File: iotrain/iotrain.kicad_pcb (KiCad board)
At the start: 2 copper layers, 24 x 14 mm, 64 parts, among them J1 12V, J10 X2, J11 SCL, J12 SDA, J13 GND, J14 3V3, J15 GND, J2 PROG ESP, J3 AC1, J4 AC1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

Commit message: ESP32-C6
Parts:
- removed U1: ESP32-C3, Package_DFN_QFN:QFN-32-1EP_5x5mm_P0.5mm_EP3.7x3.7mm
- added C20: 10u/20V, Capacitor_SMD:C_0402_1005Metric, F.Cu at (139.9, 57.5)
- added C22: 10u/20V, Capacitor_SMD:C_0402_1005Metric, F.Cu at (139.0, 57.5)
- added J16: USB_B_Micro, Connector_USB:USB_Micro-B_Amphenol_10104110_Horizontal, B.Cu at (137.3, 63.6)
- added R10: 10k, Resistor_SMD:R_0201_0603Metric, F.Cu at (128.2, 65.5)
- added U4: ESP32-C6FH4, Package_DFN_QFN:QFN-32-1EP_5x5mm_P0.5mm_EP3.6x3.6mm, F.Cu at (130.9, 61.5)
- C11, C13: value 1u -> 10u/20V; footprint Capacitor_SMD:C_0201_0603Metric -> Capacitor_SMD:C_0402_1005Metric
- J2: moved to B.Cu
- L2: value L -> 2n
- moved C11 14.7 mm to (140.9, 57.5), turned to -90 degrees
- moved C13 7.12 mm to (138.1, 57.5), turned to -90 degrees
- moved R8 5.88 mm to (141.0, 61.1)
- moved R7 5.88 mm to (140.3, 61.1)
- moved SW2 5.84 mm to (136.4, 64.2), turned to 90 degrees
- moved U6 5.70 mm to (137.6, 56.8)
- moved C25 4.66 mm to (127.2, 62.4)
- moved C21 3.84 mm to (139.6, 61.1), turned to 90 degrees
- moved C14 3.61 mm to (135.4, 61.0)
- moved R1 3.54 mm to (134.3, 60.5), turned to 90 degrees
- moved C10 2.72 mm to (126.8, 61.4), turned to 90 degrees
- moved C12 2.23 mm to (125.8, 61.6), turned to 180 degrees
- moved SW1 2.09 mm to (139.7, 64.2), turned to 90 degrees
- moved C17 1.42 mm to (137.9, 53.6), turned to -90 degrees
- moved C15 1.30 mm to (137.9, 55.5), turned to -90 degrees
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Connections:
- net Net-(U1-LNA_IN) renamed ANT
- net PROG_IO0 renamed PROG_IO9
- C11 pad 1: +3V3 -> +12V
- C13 pad 1: +3V3 -> +12V
- J2 pad 1: PROG_EN -> CHIP_EN
- R1 pad 1: PROG_TX -> Net-(U4-U0TXD/GPIO16/FSPICS0)
- R1 pad 2: Net-(U1-U0TXD) -> PROG_TX
- R5 pad 1: GND -> unconnected-(R5-Pad1)
- R6 pad 2: Net-(U1-GPIO2) -> INFO_LED
- U6 pad 1: LCD_D -> unconnected-(U6-SDA-Pad1)
- U6 pad 10: GND -> unconnected-(U6-GND-Pad10)
- U6 pad 2: LCD_C -> unconnected-(U6-SCL-Pad2)
- U6 pad 3: LCD_RS -> unconnected-(U6-RS-Pad3)
- U6 pad 4: LCD_RES -> unconnected-(U6-RES-Pad4)
- U6 pad 5: LCD_CS -> unconnected-(U6-CS-Pad5)
- U6 pad 6: GND -> unconnected-(U6-GND-Pad6)
- U6 pad 7: +3V3 -> unconnected-(U6-VCC-Pad7)
- U6 pad 8: +3V3 -> unconnected-(U6-LEDA-Pad8)
- U6 pad 9: LCD_BL -> unconnected-(U6-LEDK-Pad9)
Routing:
- net MOT_IPROPRI: track 0.00 -> 15.0 mm, vias 0 -> 2
- net Net-(J16-D-): track 0.00 -> 6.36 mm, vias 0 -> 1
- net PROG_TX: track 2.47 -> 8.17 mm, vias 0 -> 1
- net PROG_IO9: track 0.00 -> 5.50 mm
- net INFO_LED: track 0.00 -> 4.96 mm, vias 0 -> 2
- net Net-(J16-D+): track 0.00 -> 4.91 mm, vias 0 -> 1
- net CHIP_EN: track 0.00 -> 4.25 mm, vias 0 -> 1
- net PROG_RX: track 5.88 -> 9.73 mm, vias 0 -> 1
- net +3V3: track 8.27 -> 11.9 mm, vias 0 -> 2
- net Net-(U1-U0TXD): track 3.09 -> 0.00 mm
- net Net-(U1-GPIO2): track 2.26 -> 0.00 mm, vias 2 -> 0
- net Net-(C9-Pad1): track 2.23 -> 0.00 mm
- net GND: track 4.00 -> 2.15 mm, vias 1 -> 0
- net PROG_EN: track 0.00 -> 1.66 mm
- net MOT_EN: track 10.5 -> 8.89 mm
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
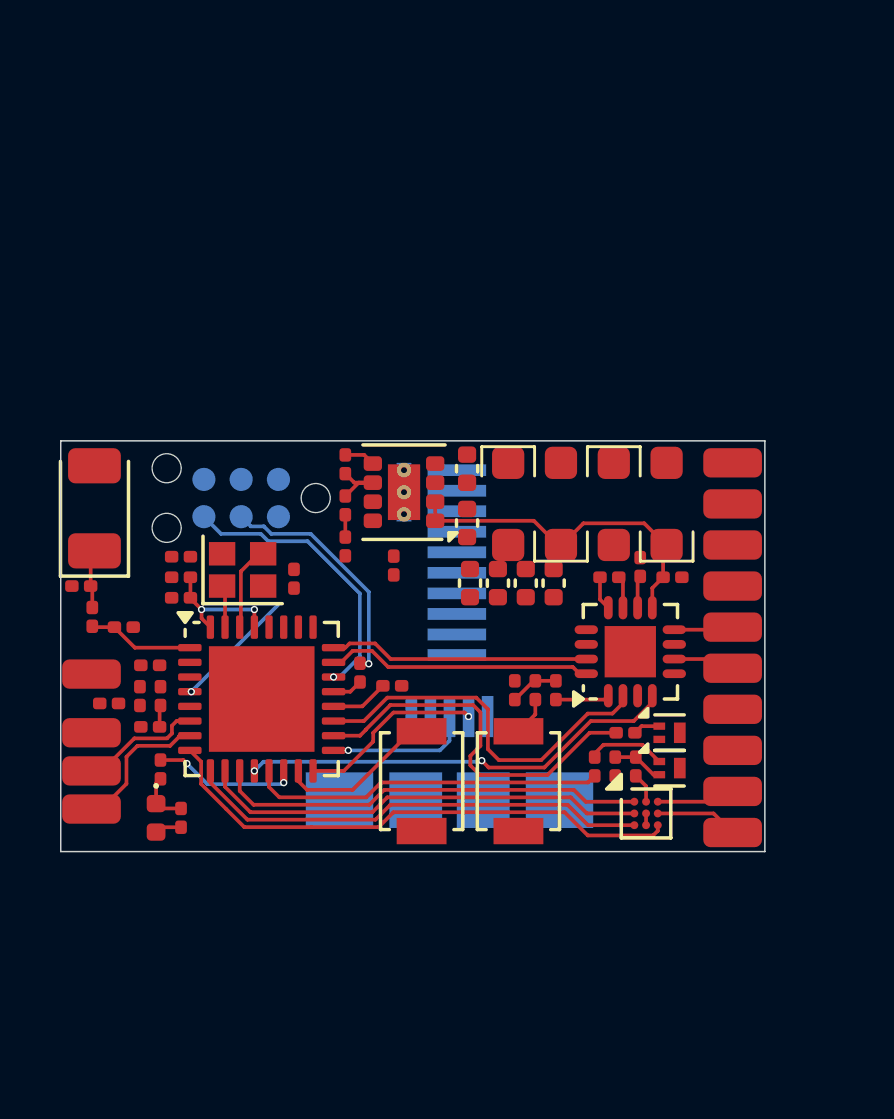
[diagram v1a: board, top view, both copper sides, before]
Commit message: Slightly improved placement -->22x14mm
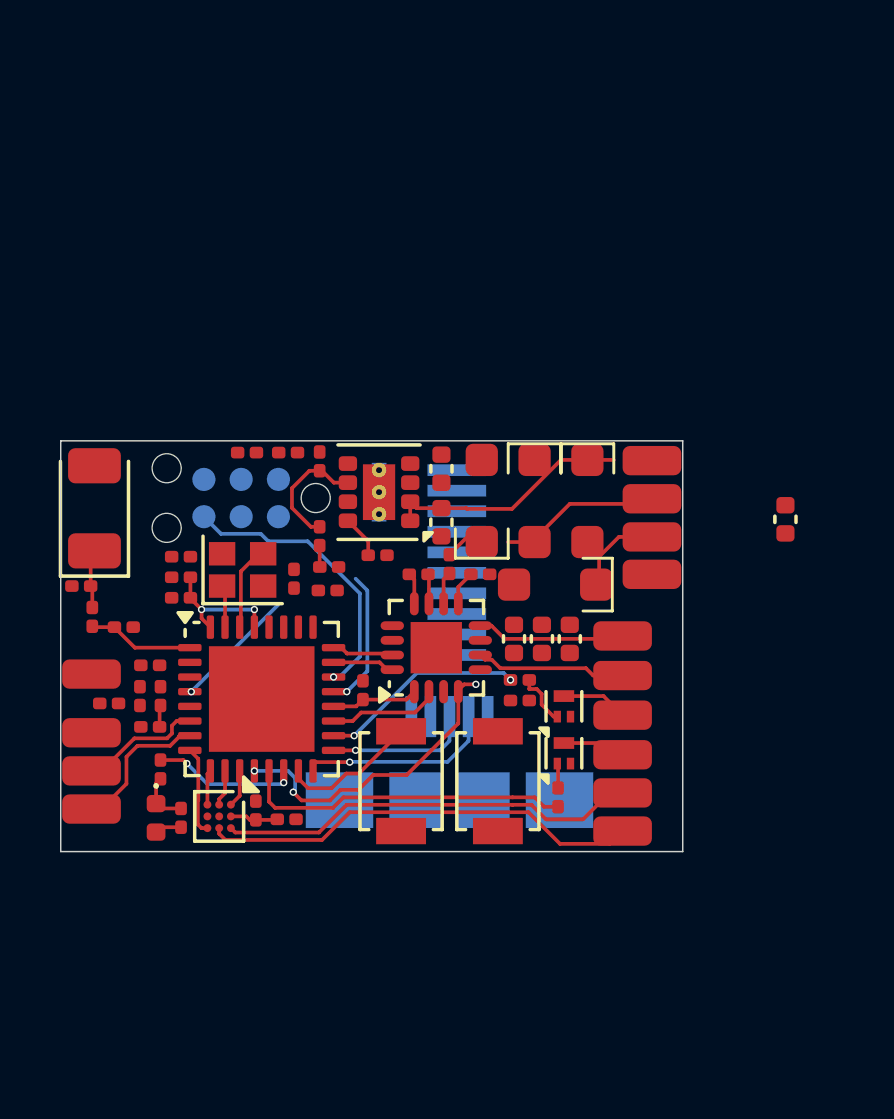
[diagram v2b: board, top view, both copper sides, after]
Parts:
- moved U2 14.6 mm to (129.5, 65.5), turned to -90 degrees
- moved C19 12.3 mm to (130.8, 65.2)
- moved C21 12.2 mm to (130.4, 53.0), turned to 180 degrees
- moved R8 12.2 mm to (131.8, 53.0), turned to 0 degrees
- moved C18 12.0 mm to (131.8, 65.5), turned to 0 degrees
- moved C22 10.0 mm to (148.8, 55.3)
- moved U7 6.61 mm to (136.9, 59.7)
- moved C7 6.55 mm to (138.4, 57.2)
- moved C26 6.50 mm to (137.3, 56.9)
- moved C8 6.50 mm to (136.3, 57.2)
- moved R9 4.02 mm to (139.8, 60.8)
- moved J1 3.98 mm to (144.2, 53.3)
- moved C13 3.89 mm to (141.4, 59.4)
- moved J8 3.76 mm to (143.2, 59.3)
- moved J7 3.76 mm to (143.2, 60.6)
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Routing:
- net I2S_LR: track 18.3 -> 3.03 mm
- net I2S_BCLK: track 15.9 -> 1.19 mm
- net I2S_DIN: track 15.3 -> 1.23 mm
- net I2S_SD: track 14.7 -> 1.27 mm
- net /LSPN: track 2.82 -> 15.0 mm
- net /LSPP: track 2.69 -> 14.4 mm
- net MOT_FAULT: track 12.9 -> 3.80 mm
- net PROG_TX: track 8.17 -> 0.00 mm, vias 1 -> 0
- net MOT_PH: track 9.10 -> 2.08 mm
- net MOT_EN: track 8.89 -> 2.08 mm
- net T2: track 13.2 -> 7.01 mm, vias 0 -> 2
- net /AC2: track 0.00 -> 5.51 mm
- net MOT_IPROPRI: track 15.0 -> 10.6 mm, vias 2 -> 3
- net Net-(U4-U0TXD/GPIO16/FSPICS0): track 1.04 -> 4.76 mm, vias 0 -> 1
- net /M2: track 2.01 -> 5.08 mm
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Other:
- board size 24 x 14 mm -> 21.2 x 14 mm

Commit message: Make it smaller
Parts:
- removed C13: 10u/20V, Capacitor_SMD:C_0402_1005Metric
- added R11: 1k, liebler_PASSIVES:SMD0201, F.Cu at (126.9, 63.1)
- added R12: 1k, liebler_PASSIVES:SMD0201, F.Cu at (127.7, 63.6)
- C1, C10, C14, C16, C19, C2, C21, C25, C26, C3, C4, C5, C6, C7, C8, C9: footprint Capacitor_SMD:C_0201_0603Metric -> liebler_PASSIVES:SMD0201
- C11: footprint Capacitor_SMD:C_0402_1005Metric -> Capacitor_SMD:C_0805_2012Metric
- C12, C18: footprint Capacitor_SMD:C_0201_0603Metric -> liebler_PASSIVES:SMD0402
- C15, C17, C20, C22: footprint Capacitor_SMD:C_0402_1005Metric -> liebler_PASSIVES:SMD0402
- L1, L2: footprint Inductor_SMD:L_0201_0603Metric -> liebler_PASSIVES:SMD0201
- R1, R10, R2, R3, R4, R5, R6, R7, R8, R9: footprint Resistor_SMD:R_0201_0603Metric -> liebler_PASSIVES:SMD0201
- SW1, SW2: footprint Button_Switch_SMD:SW_SPST_B3U-1000P -> liebler_MECH:SW_SPST_TL3342_smaller_handsolder; moved to B.Cu
- moved U6 14.0 mm to (139.8, 43.0)
- moved R7 13.2 mm to (129.4, 53.3), turned to -90 degrees
- moved C22 12.5 mm to (138.6, 62.5)
- moved SW1 9.08 mm to (139.7, 55.2), turned to 0 degrees
- moved SW2 8.98 mm to (127.0, 61.9), turned to -90 degrees
- moved J16 8.12 mm to (135.5, 71.5)
- moved C11 7.69 mm to (133.2, 57.1), turned to 180 degrees
- moved R4 7.43 mm to (133.6, 64.6), turned to 0 degrees
- moved C17 6.49 mm to (130.6, 53.2), turned to 180 degrees
- moved Q2 5.74 mm to (135.7, 63.0), turned to 0 degrees
- moved R9 5.72 mm to (134.3, 62.7)
- moved Q1 5.66 mm to (135.7, 64.2), turned to 0 degrees
- moved D5 5.43 mm to (139.7, 60.0), turned to -90 degrees
- moved R1 4.64 mm to (129.2, 55.4), turned to 0 degrees
- moved D3 4.64 mm to (138.6, 53.5)
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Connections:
- C21 pad 1: PROG_EN -> CHIP_EN
- R5 pad 1: unconnected-(R5-Pad1) -> GND
- R7 pad 2: PROG_EN -> CHIP_EN
- R8 pad 1: PROG_EN -> CHIP_EN
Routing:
- net Net-(R7-Pad1): track 0.00 -> 14.4 mm, vias 0 -> 1
- net T1: track 11.3 -> 2.65 mm
- net GND: track 0.85 -> 9.14 mm, vias 0 -> 4
- net CHIP_EN: track 4.25 -> 12.0 mm, vias 1 -> 3
- net Net-(J16-D-): track 6.74 -> 0.00 mm, vias 1 -> 0
- net T2: track 7.01 -> 0.67 mm, vias 2 -> 0
- net +3V3: track 10.6 -> 16.5 mm, vias 2 -> 3
- net /X2: track 2.27 -> 7.27 mm
- net Net-(J16-D+): track 4.91 -> 0.00 mm, vias 1 -> 0
- net PROG_IO9: track 4.70 -> 0.00 mm
- net Net-(U4-U0TXD/GPIO16/FSPICS0): track 4.76 -> 9.39 mm, vias 1 -> 2
- net /X1: track 2.17 -> 6.55 mm
- net MOT_IPROPRI: track 10.6 -> 7.21 mm, vias 3 -> 2
- net Net-(U3-FB): track 4.20 -> 1.45 mm
- net /LSPP: track 14.4 -> 12.0 mm, vias 0 -> 2
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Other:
- board size 21.2 x 14 mm -> 19 x 13.8 mm

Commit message: various
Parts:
- added C3: 1u, liebler_PASSIVES:SMD0201, F.Cu at (133.3, 57.6)
- added C4: 10n, liebler_PASSIVES:SMD0201, F.Cu at (133.3, 56.6)
- added D6: XL-1010RGBC-WS2812B, liebler_OPTO:XL-1010RGBC-WS2812B, F.Cu at (132.3, 57.8)
- added D7: XL-1010RGBC-WS2812B, liebler_OPTO:XL-1010RGBC-WS2812B, F.Cu at (132.3, 56.3)
- AE1: value Antenna_Chip -> Antenna
- C11: value 10u/20V -> 22u/25V; footprint Capacitor_SMD:C_0805_2012Metric -> liebler_PASSIVES:SMD0805
- C15, C20, C22: value 10u/20V -> 10u/25V; footprint liebler_PASSIVES:SMD0402 -> liebler_PASSIVES:SMD0603
- SW1, SW2: footprint liebler_MECH:SW_SPST_TL3342_smaller_handsolder -> Button_Switch_SMD:SW_Push_SPST_NO_Alps_SKRK
- moved C11 16.7 mm to (149.8, 58.4), turned to -90 degrees
- moved C22 9.28 mm to (146.9, 58.5), turned to 180 degrees
- moved C20 6.83 mm to (144.6, 62.7)
- moved Q1 4.11 mm to (139.8, 63.8)
- moved Q2 4.11 mm to (139.8, 62.6)
- moved SW2 3.23 mm to (130.2, 62.5), turned to 0 degrees
- moved C16 1.51 mm to (131.3, 55.2)
- moved C15 0.82 mm to (134.9, 56.7)
- moved C8 0.06 mm to (135.4, 57.5)
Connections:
- R8 pad 1: CHIP_EN -> +3V3
- R8 pad 2: +3V3 -> CHIP_EN
- U4 pad 25: unconnected-(U4-GPIO20/SDIO_DATA0/FSPICS4-Pad25) -> RGB_LED
- U6 pad 1: unconnected-(U6-SDA-Pad1) -> LCD_D
- U6 pad 10: unconnected-(U6-GND-Pad10) -> GND
- U6 pad 2: unconnected-(U6-SCL-Pad2) -> LCD_C
- U6 pad 3: unconnected-(U6-RS-Pad3) -> LCD_RS
- U6 pad 4: unconnected-(U6-RES-Pad4) -> LCD_RES
- U6 pad 5: unconnected-(U6-CS-Pad5) -> LCD_CS
- U6 pad 6: unconnected-(U6-GND-Pad6) -> GND
- U6 pad 7: unconnected-(U6-VCC-Pad7) -> +3V3
- U6 pad 8: unconnected-(U6-LEDA-Pad8) -> +3V3
- U6 pad 9: unconnected-(U6-LEDK-Pad9) -> LCD_BL
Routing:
- net CHIP_EN: track 12.0 -> 3.33 mm, vias 3 -> 1
- net /X2: track 7.27 -> 2.39 mm
- net /X1: track 6.55 -> 2.26 mm
- net Net-(Q1-G): track 1.67 -> 5.91 mm
- net Net-(Q2-G): track 0.69 -> 4.91 mm
- net +12V: track 9.05 -> 6.30 mm
- net GND: track 9.14 -> 7.49 mm
- net Net-(U3-SS/TR): track 0.83 -> 2.32 mm
- net RGB_LED: track 0.00 -> 0.84 mm
- net Net-(D6-DOUT): track 0.00 -> 0.62 mm
- net /LSPN: track 12.9 -> 12.3 mm
